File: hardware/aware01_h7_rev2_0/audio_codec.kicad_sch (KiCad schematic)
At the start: 15 parts, among them IC5 TLV320AIC3204IRHBR

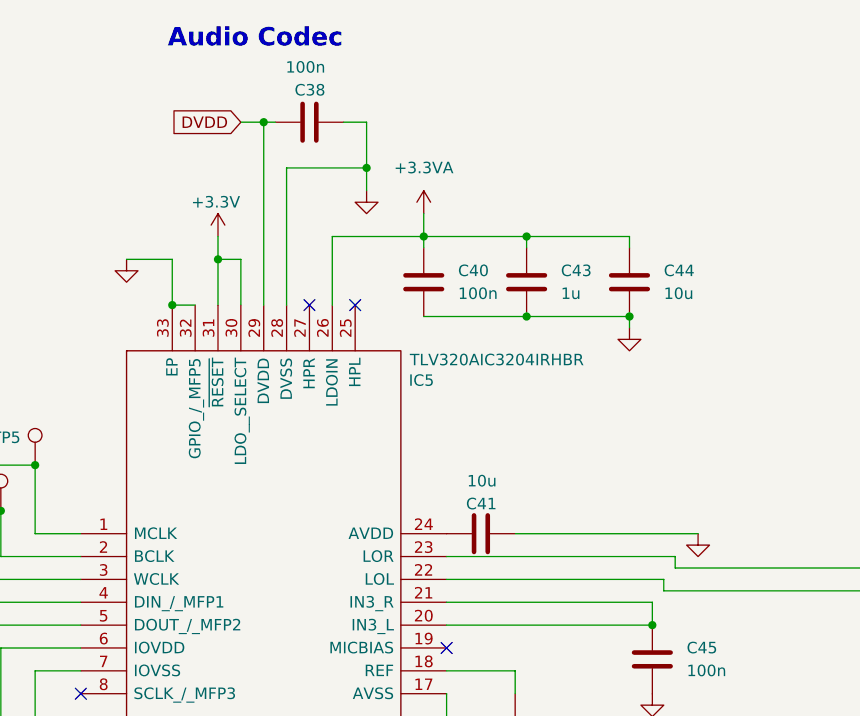
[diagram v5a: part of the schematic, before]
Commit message: hardware: change clamping reference to codec AVDD
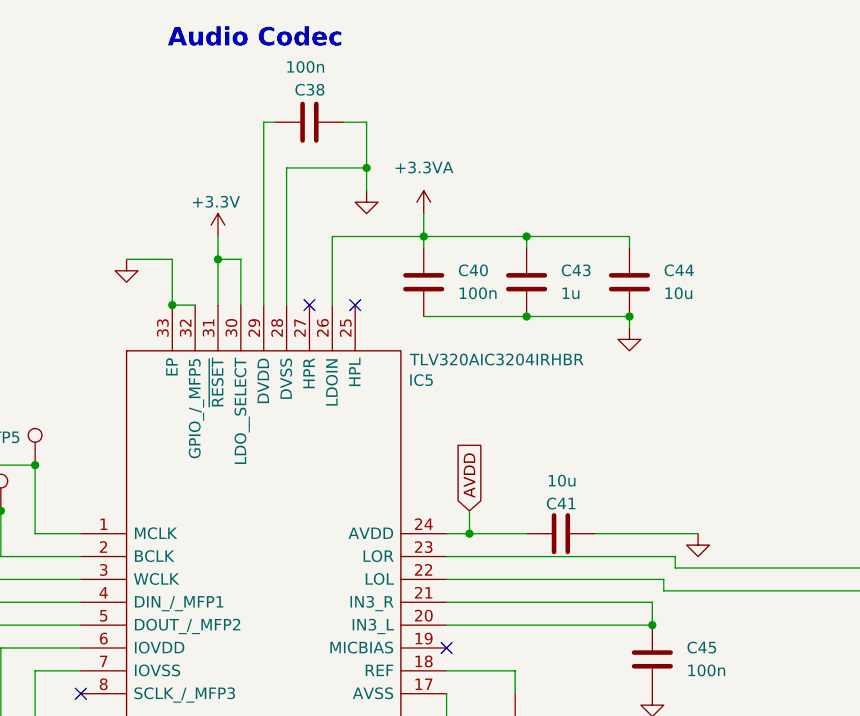
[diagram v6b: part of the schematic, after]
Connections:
- net AVDD: now reaches C41.2, IC5.24 (AVDD)
- net DVDD: no longer names the net of C38.2, IC5.29 (DVDD)
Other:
- moved on the sheet: C41
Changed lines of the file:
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@@
-	)
-	(junction
-		(at 119.38 39.37)
-		(diameter 0)
-		(color 0 0 0 0)
 	)
 	(junction
@@
 	)
 	(junction
+		(at 142.24 85.09)
+		(diameter 0)
+		(color 0 0 0 0)
+	)
+	(junction
 		(at 130.81 44.45)
 		(diameter 0)
@@
 	(wire
 		(pts
+			(xy 142.24 85.09) (xy 139.7 85.09)
+		)
+		(stroke
+			(width 0)
+			(type default)
+		)
+	)
+	(wire
+		(pts
 			(xy 119.38 39.37) (xy 119.38 59.69)
 		)
@@
 	(wire
 		(pts
+			(xy 142.24 82.55) (xy 142.24 85.09)
+		)
+		(stroke
+			(width 0)
+			(type default)
+		)
+	)
+	(wire
+		(pts
 			(xy 121.92 44.45) (xy 121.92 59.69)
 		)
@@
 	(wire
 		(pts
+			(xy 148.59 85.09) (xy 142.24 85.09)
+		)
+		(stroke
+			(width 0)
+			(type default)
+		)
+	)
+	(wire
+		(pts
 			(xy 90.17 111.76) (xy 90.17 97.79)
 		)
@@
 	(wire
 		(pts
-			(xy 167.64 85.09) (xy 147.32 85.09)
+			(xy 167.64 85.09) (xy 156.21 85.09)
 		)
 		(stroke
@@
 	(wire
 		(pts
-			(xy 116.84 39.37) (xy 119.38 39.37)
-		)
-		(stroke
-			(width 0)
-			(type default)
-		)
-	)
-	(wire
-		(pts
 			(xy 148.59 52.07) (xy 148.59 53.34)
 		)
@@
 		)
 	)
-	(global_label "DVDD"
+	(global_label "AVDD"
 		(shape input)
-		(at 116.84 39.37 180)
+		(at 142.24 82.55 90)
 		(fields_autoplaced yes)
 		(effects
@@
 				(size 1.27 1.27)
 			)
-			(justify right)
+			(justify left)
 		)
 		(property "Intersheetrefs" "${INTERSHEET_REFS}"
-			(at 108.9562 39.37 0)
-			(effects
-				(font
-					(size 1.27 1.27)
-				)
-				(justify right)
+			(at 142.24 74.8476 90)
+			(effects
+				(font
+					(size 1.27 1.27)
+				)
+				(justify left)
 				(hide yes)
 			)
@@
 	(symbol
 		(lib_id "Device:C")
-		(at 143.51 85.09 270)
+		(at 152.4 85.09 270)
 		(unit 1)
 		(exclude_from_sim no)
@@
 		(dnp no)
 		(property "Reference" "C41"
-			(at 145.288 81.788 90)
+			(at 154.178 81.788 90)
 			(effects
 				(font
@@
 		)
 		(property "Value" "10u"
-			(at 145.288 79.248 90)
+			(at 154.178 79.248 90)
 			(effects
 				(font
@@
 		)
 		(property "Footprint" "Capacitor_SMD:C_0603_1608Metric"
-			(at 139.7 86.0552 0)
+			(at 148.59 86.0552 0)
 			(effects
 				(font
@@
 		)
 		(property "Datasheet" "~"
-			(at 143.51 85.09 0)
+			(at 152.4 85.09 0)
 			(effects
 				(font
@@
 		)
 		(property "Description" "Unpolarized capacitor"
-			(at 143.51 85.09 0)
+			(at 152.4 85.09 0)
 			(effects
 				(font
@@
 		)
 		(property "Manufacturer_Name" "Murata Electronics "
-			(at 143.51 85.09 0)
+			(at 152.4 85.09 0)
 			(effects
 				(font
@@
 		)
 		(property "Manufacturer_Part_Number" " GRM188R61E106KA73D "
-			(at 143.51 85.09 0)
+			(at 152.4 85.09 0)
 			(effects
 				(font
@@
 		)
 		(property "Mouser Part Number" " 81-GRM188R61E106KA3D "
-			(at 143.51 85.09 0)
-			(effects
-				(font
+			(at 152.4 85.09 0)
+			(effects
+				(font

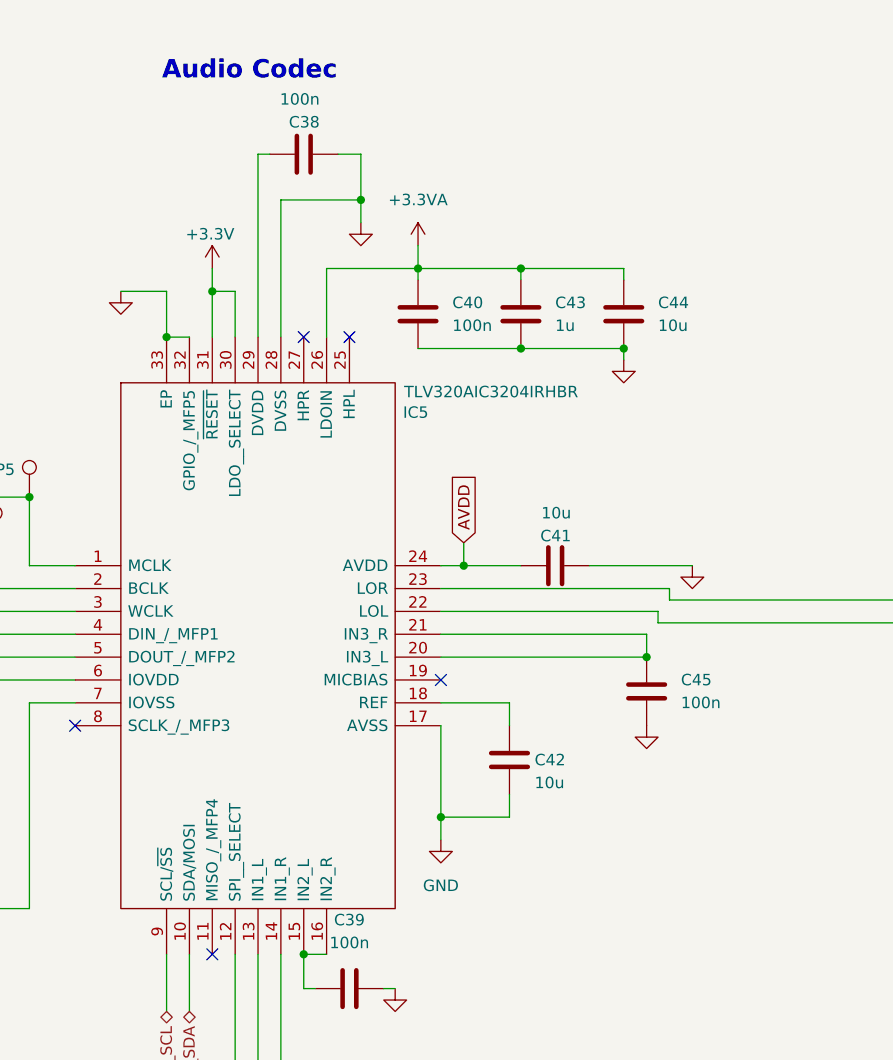
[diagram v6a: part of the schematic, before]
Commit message: hw: improve layout, update BOM
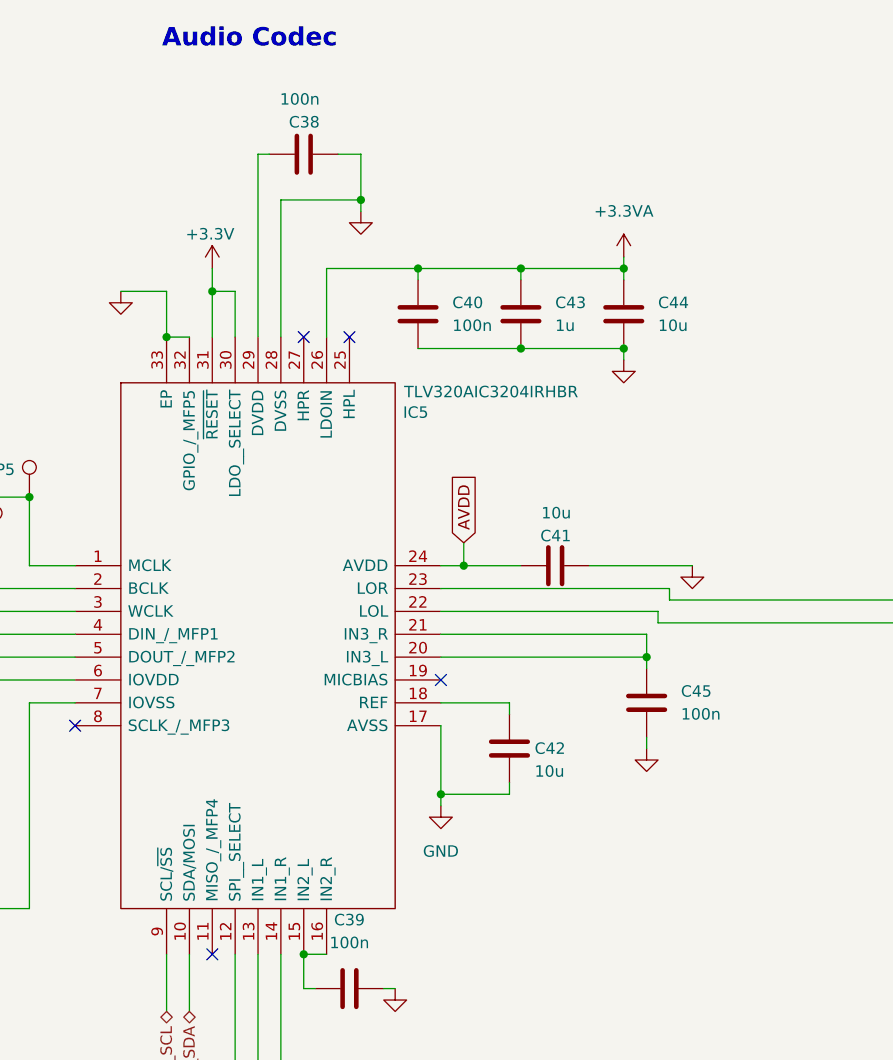
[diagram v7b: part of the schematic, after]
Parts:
- TP1, TP2, TP3, TP4, TP5: now left out of the parts list
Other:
- moved on the sheet: C42, C45

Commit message: hw: update BOM and layout
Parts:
- C41, C42: Manufacturer_Part_Number GRM188R61E106KA73D -> GRM188R61E106KA73D
- C43: Manufacturer_Part_Number KAF15BR72A104KT -> KGM15AV51A105ZM; Mouser Part Number 581-KAF15BR72A104KT -> 581-KGM15AV51A105ZM
- C44: Manufacturer_Name KYOCERA AVX -> Murata Electronics; Manufacturer_Part_Number KAF15BR72A104KT -> GRM188R61E106KA73D; Mouser Part Number 581-KAF15BR72A104KT -> 81-GRM188R61E106KA3D
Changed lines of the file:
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@@
 			)
 		)
-		(property "Manufacturer_Name" "KYOCERA AVX "
+		(property "Manufacturer_Name" "Murata Electronics "
 			(at 160.02 57.15 0)
 			(effects
@@
 			)
 		)
-		(property "Manufacturer_Part_Number" "KAF15BR72A104KT"
+		(property "Manufacturer_Part_Number" "GRM188R61E106KA73D"
 			(at 160.02 57.15 0)
 			(effects
@@
 			)
 		)
-		(property "Mouser Part Number" "581-KAF15BR72A104KT"
+		(property "Mouser Part Number" " 81-GRM188R61E106KA3D "
 			(at 160.02 57.15 0)
 			(effects
@@
 			)
 		)
-		(property "Manufacturer_Part_Number" " GRM188R61E106KA73D "
+		(property "Manufacturer_Part_Number" "GRM188R61E106KA73D"
 			(at 147.32 105.41 0)
 			(effects
@@
 			)
 		)
-		(property "Manufacturer_Part_Number" " GRM188R61E106KA73D "
+		(property "Manufacturer_Part_Number" "GRM188R61E106KA73D"
 			(at 152.4 85.09 0)
 			(effects
@@
 			)
 		)
-		(property "Manufacturer_Part_Number" "KAF15BR72A104KT"
+		(property "Manufacturer_Part_Number" "KGM15AV51A105ZM "
 			(at 148.59 57.15 0)
 			(effects
@@
 			)
 		)
-		(property "Mouser Part Number" "581-KAF15BR72A104KT"
+		(property "Mouser Part Number" "581-KGM15AV51A105ZM"
 			(at 148.59 57.15 0)
 			(effects
